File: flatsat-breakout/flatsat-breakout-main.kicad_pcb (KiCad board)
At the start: 2 copper layers, 34 x 94 mm, 9 parts, among them J1 Conn_01x40, J2 Conn_01x40, J3 Conn_01x40, J4 Conn_01x27, J5 Conn_02x08_Odd_Even

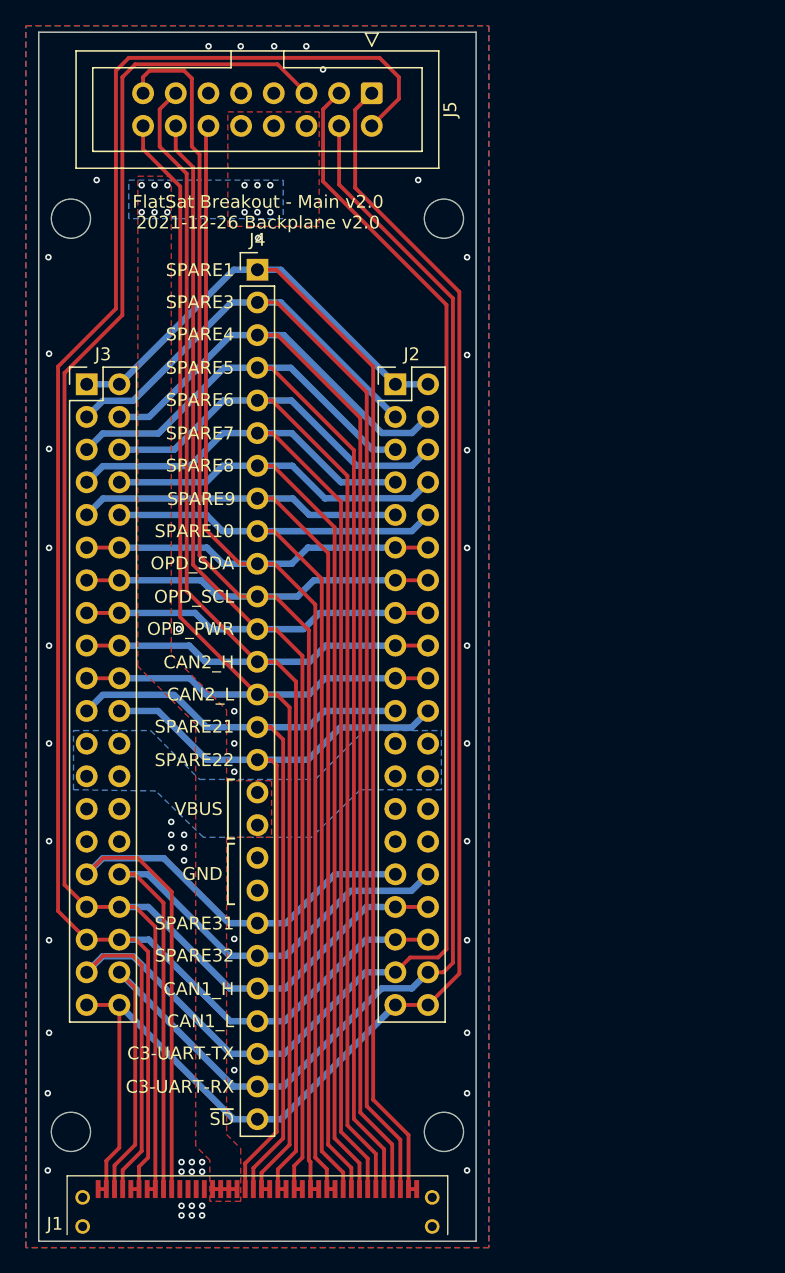
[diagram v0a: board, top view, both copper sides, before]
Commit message: Updated FlatSat breakout and backplane debug board layouts after design review
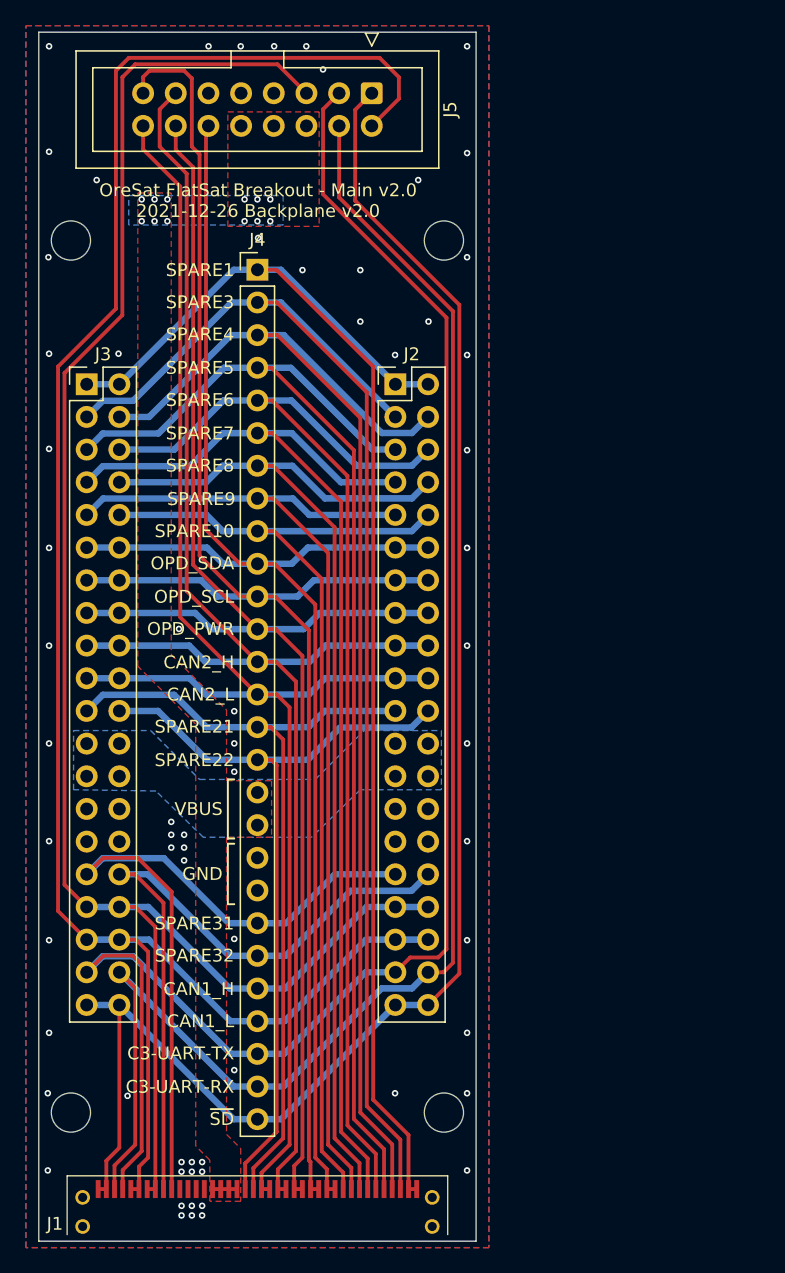
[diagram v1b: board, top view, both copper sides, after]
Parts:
- moved REF** 1.70 mm to (164.5, 64.7)
- moved REF** 1.70 mm to (135.5, 64.7)
- moved REF** 1.50 mm to (135.5, 132.5)
- moved REF** 1.50 mm to (164.5, 132.5)
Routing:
- net GND: vias 54 -> 66
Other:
- board text added: "OreSat FlatSat Breakout - Main v2.0 2021-12-26 Backplane v2.0"
- board text removed: "FlatSat Breakout - Main v2.0 2021-12-26 Backplane v2.0"

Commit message: Fixed signal name silkscreen covered by connector footprint
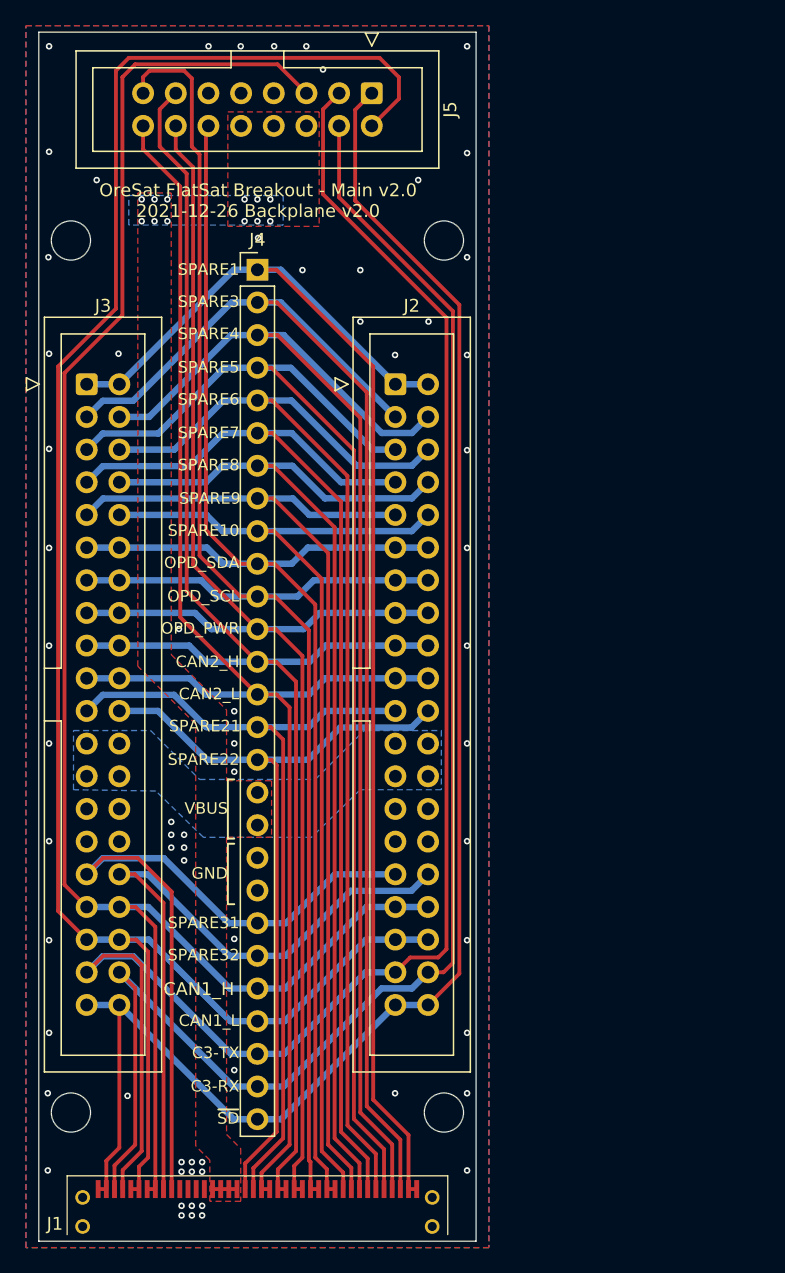
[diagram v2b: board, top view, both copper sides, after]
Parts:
- J2, J3: footprint Connector_PinHeader_2.54mm:PinHeader_2x20_P2.54mm_Vertical -> Connector_IDC:IDC-Header_2x20_P2.54mm_Vertical
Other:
- board text added: "C3-RX"
- board text added: "C3-TX"
- board text removed: "C3-UART-RX"
- board text removed: "C3-UART-TX"

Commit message: Updated to latest KiCAD, added BOM info to parts, updated 3D model, cleaned up silkscreen, rounded board edges.
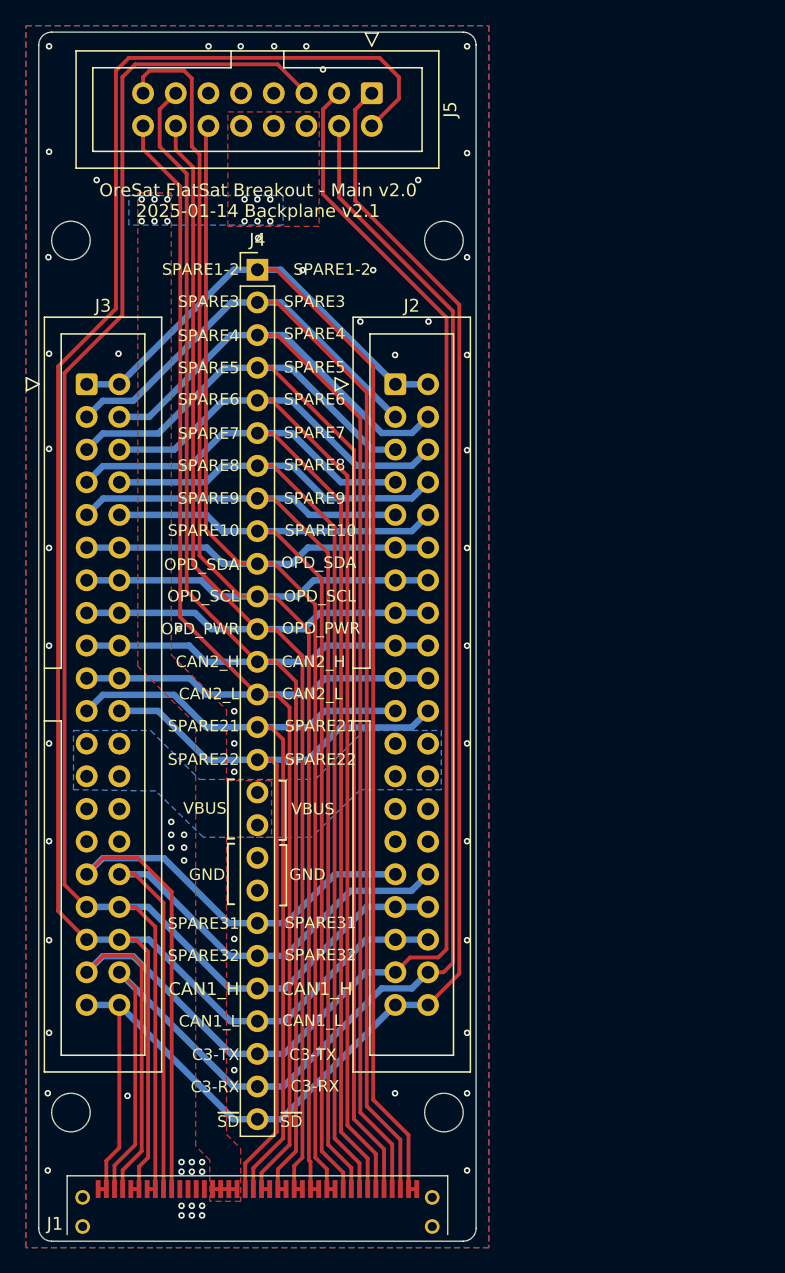
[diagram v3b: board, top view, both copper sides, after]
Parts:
- J1: value Conn_01x40 -> SFM-120-02-L-DH-TR; footprint J-SAMTEC-SFM-120-02-X-DH:SFM-120-02-X-DH -> oresat-connectors:SFM-120-02-X-DH
- J4: value Conn_01x27 -> 68000-227HLF
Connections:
- J1 pad G1: GND -> (no net)
- J1 pad G2: GND -> (no net)
- J1 pad G3: GND -> (no net)
- J1 pad G4: GND -> (no net)
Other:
- outline, holes or cut-outs redrawn
- board text added: "OreSat FlatSat Breakout - Main v2.0 2025-01-14 Backplane v2.1"
- board text added: "SPARE1-2"
- board text removed: "OreSat FlatSat Breakout - Main v2.0 2021-12-26 Backplane v2.0"
- board text removed: "SPARE1"

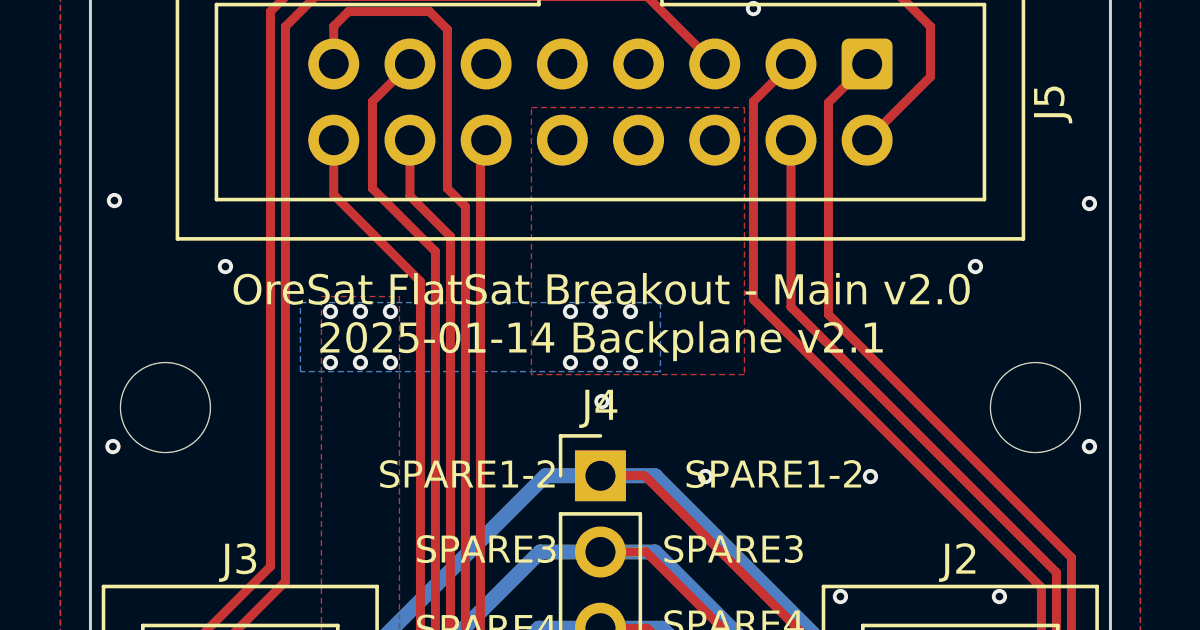
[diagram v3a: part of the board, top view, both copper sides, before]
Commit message: Fixes versioning (now v2.1)
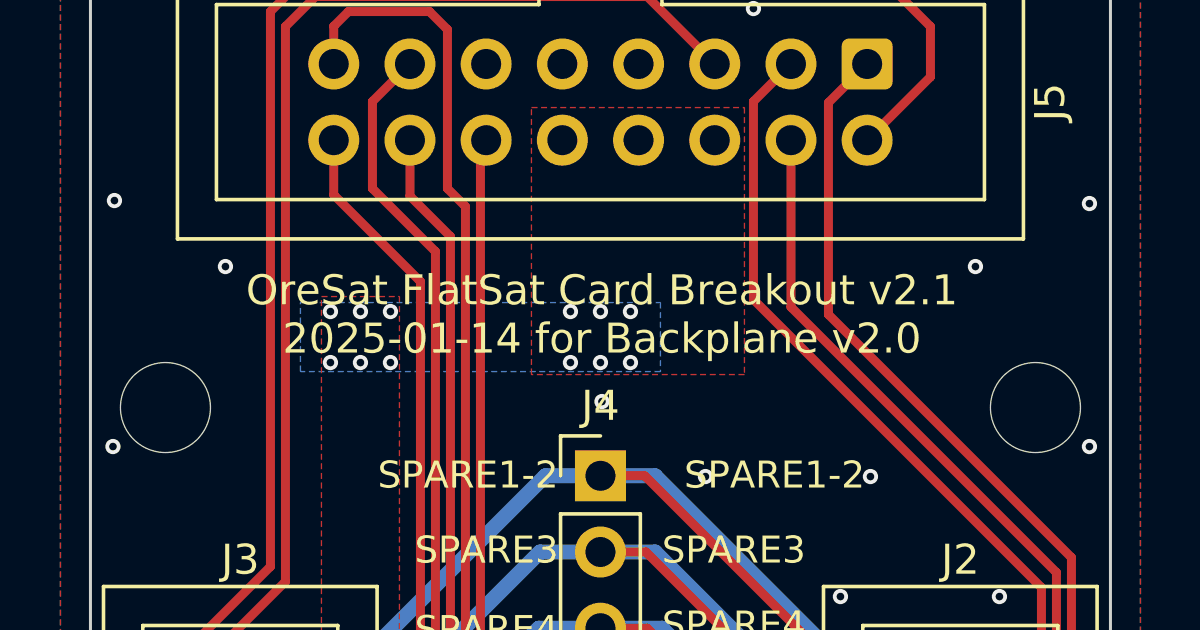
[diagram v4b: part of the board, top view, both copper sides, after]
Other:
- board text added: "OreSat FlatSat Card Breakout v2.1 2025-01-14 for Backplane v2.0"
- board text removed: "OreSat FlatSat Breakout - Main v2.0 2025-01-14 Backplane v2.1"
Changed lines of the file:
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@@
 		(legacy_teardrops no)
 	)
-	(paper "A4")
+	(paper "USLedger")
+	(title_block
+		(date "2025-01-13")
+		(rev "2.1")
+	)
 	(layers
 		(0 "F.Cu" signal)
@@
 		)
 	)
-	(gr_text "OreSat FlatSat Breakout - Main v2.0\n2025-01-14 Backplane v2.1"
+	(gr_text "OreSat FlatSat Card Breakout v2.1\n2025-01-14 for Backplane v2.0"
 		(at 150.05 61.6 0)
 		(layer "F.SilkS")

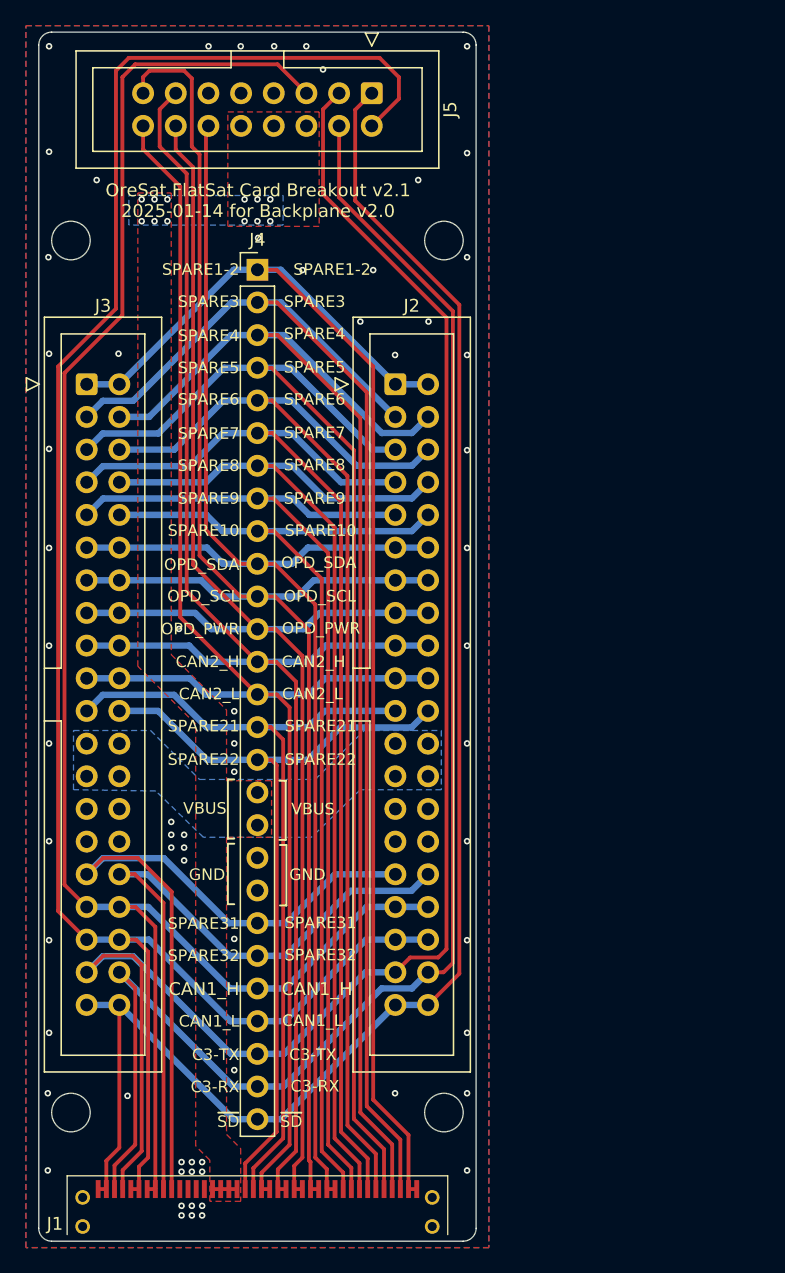
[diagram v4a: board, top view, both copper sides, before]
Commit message: Update PCB based on new schematic
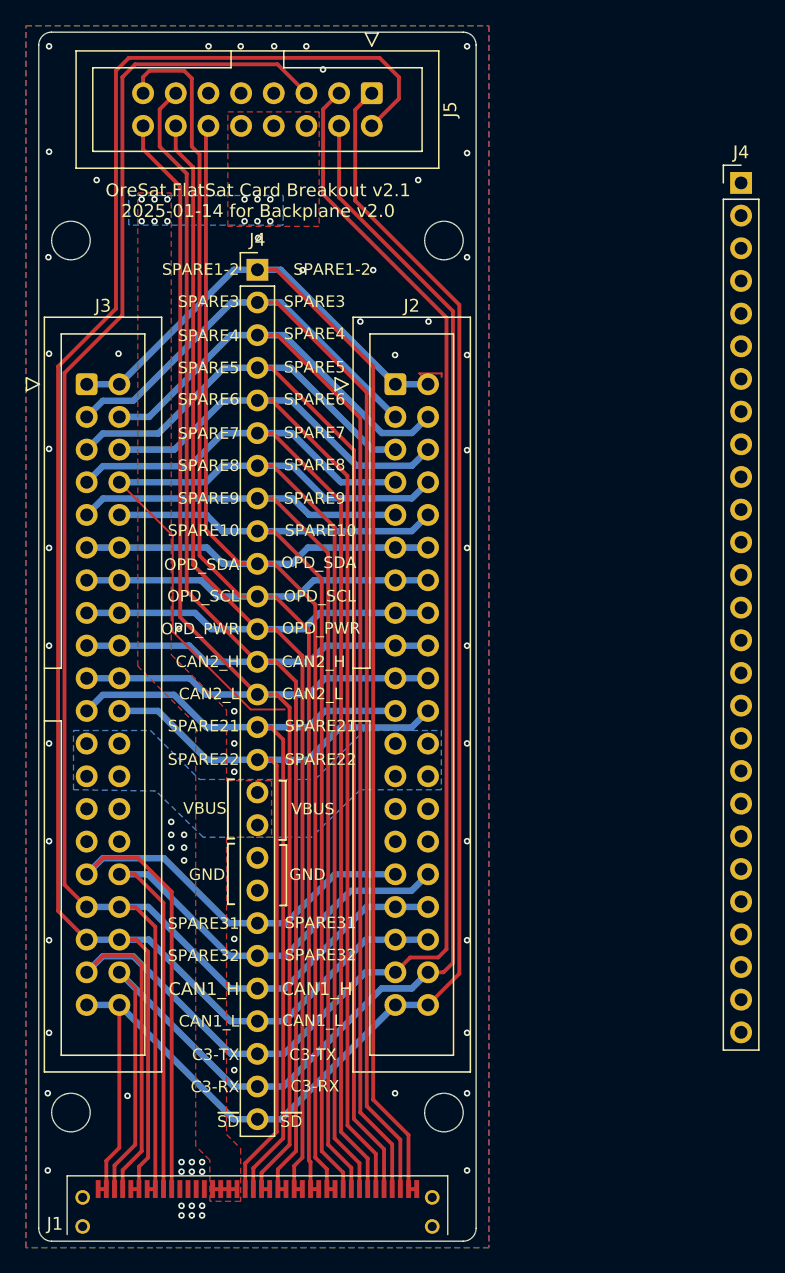
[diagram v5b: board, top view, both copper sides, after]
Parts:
- added J4: 68000-227HLF, Connector_PinHeader_2.54mm:PinHeader_1x27_P2.54mm_Vertical, F.Cu at (187.6, 60.2)
- J2, J3: value Conn_01x40 -> 61204021621
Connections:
- J1 pad 1: /SPARE1 -> /MAG-SDA
- J1 pad 10: /SPARE10 -> /TURNSTILE-DEPLOY
- J1 pad 2: /SPARE1 -> /MAG-SDA
- J1 pad 3: /SPARE3 -> /MAG-SCL
- J1 pad 4: /SPARE4 -> /MAG-SCL
- J1 pad 5: /SPARE5 -> /MAG-POWER
- J1 pad 6: /SPARE6 -> /MAG-POWER
- J1 pad 7: /SPARE7 -> /HELICAL-DEPLOY
- J1 pad 8: /SPARE8 -> /HELICAL-DEPLOY
- J1 pad 9: /SPARE9 -> /TURNSTILE-DEPLOY
- J2 pad 1: /SPARE1 -> /MAG-SDA
- J2 pad 10: /SPARE10 -> /TURNSTILE-DEPLOY
- J2 pad 2: /SPARE1 -> /MAG-SDA
- J2 pad 3: /SPARE3 -> /MAG-SCL
- J2 pad 4: /SPARE4 -> /MAG-SCL
- J2 pad 5: /SPARE5 -> /MAG-POWER
- J2 pad 6: /SPARE6 -> /MAG-POWER
- J2 pad 7: /SPARE7 -> /HELICAL-DEPLOY
- J2 pad 8: /SPARE8 -> /HELICAL-DEPLOY
- J2 pad 9: /SPARE9 -> /TURNSTILE-DEPLOY
- J3 pad 1: /SPARE1 -> /MAG-SDA
- J3 pad 10: /SPARE10 -> /TURNSTILE-DEPLOY
- J3 pad 2: /SPARE1 -> /MAG-SDA
- J3 pad 3: /SPARE3 -> /MAG-SCL
- J3 pad 4: /SPARE4 -> /MAG-SCL
- J3 pad 5: /SPARE5 -> /MAG-POWER
- J3 pad 6: /SPARE6 -> /MAG-POWER
- J3 pad 7: /SPARE7 -> /HELICAL-DEPLOY
- J3 pad 8: /SPARE8 -> /HELICAL-DEPLOY
- J3 pad 9: /SPARE9 -> /TURNSTILE-DEPLOY
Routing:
- net /HELICAL-DEPLOY: track 0.00 -> 24.5 mm
- net /MAG-SDA: track 0.00 -> 3.14 mm
